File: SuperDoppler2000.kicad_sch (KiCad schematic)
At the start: 5 parts, among them U1 TPS7A0533PDBZ

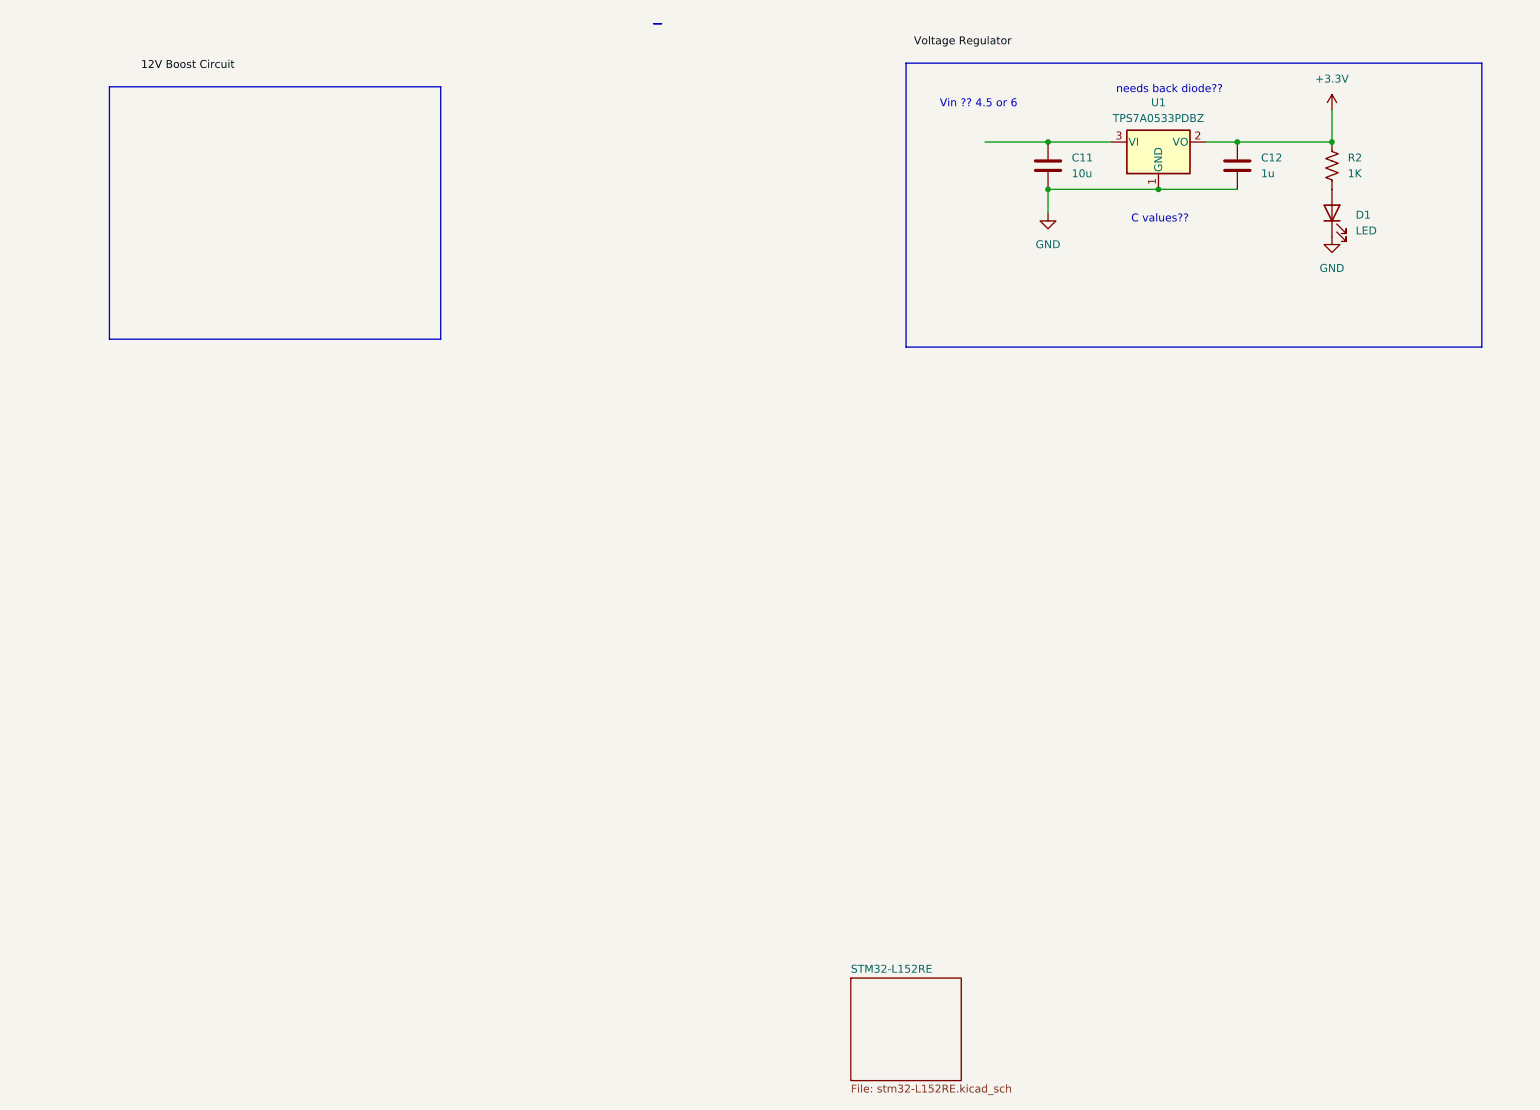
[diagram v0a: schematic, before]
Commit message: add buck
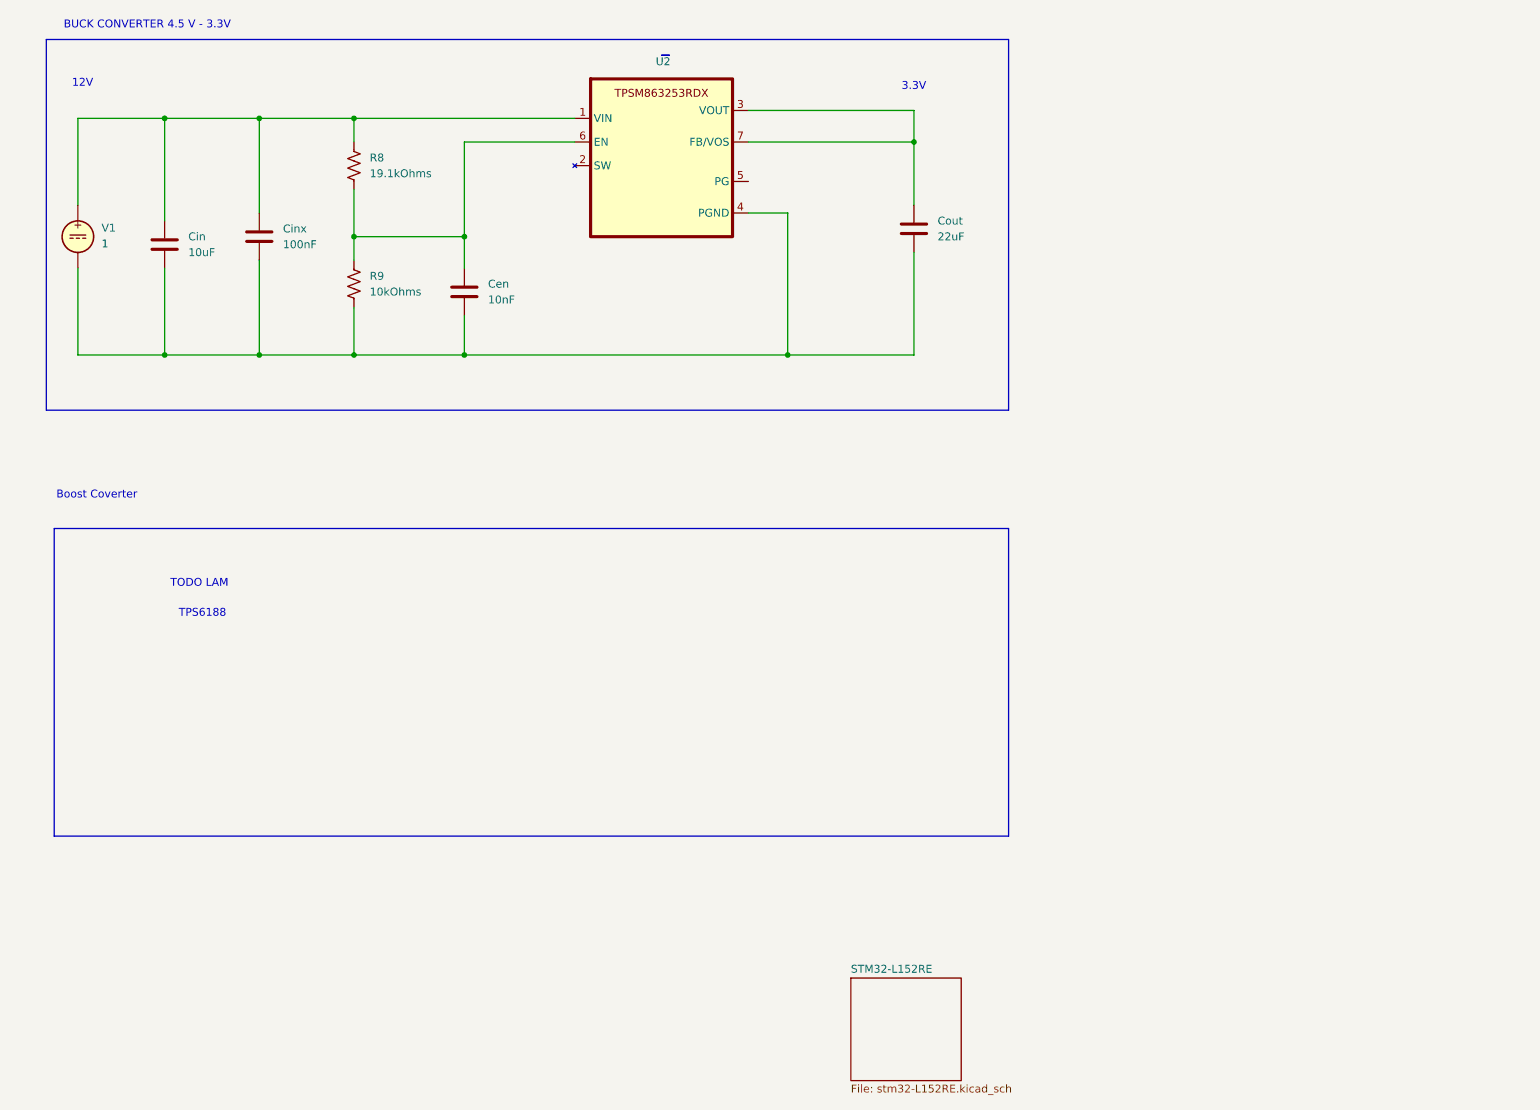
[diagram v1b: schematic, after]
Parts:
- removed C11: 10u, symbol Device:C
- removed C12: 1u, symbol Device:C
- removed D1: LED, symbol Device:LED
- removed R2: 1K, symbol Device:R_US
- removed U1: TPS7A0533PDBZ, Package_TO_SOT_SMD:SOT-23, symbol Regulator_Linear:TPS7A0533PDBZ
- added Cen: 10nF, symbol Device:C
- added Cin: 10uF, Capacitor_THT:C_Disc_D3.0mm_W1.6mm_P2.50mm, symbol Device:C
- added Cinx: 100nF, Capacitor_THT:C_Disc_D3.0mm_W1.6mm_P2.50mm, symbol Device:C
- added Cout: 22uF, symbol Device:C
- added R8: 19.1kOhms, symbol Device:R_US
- added R9: 10kOhms, symbol Device:R_US
- added U2: ~, symbol 2_Converter_DCDC:TPSM863253RDX
- added V1: 1, symbol Simulation_SPICE:VDC
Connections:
- new net: Cen.1, R8.2, R9.1, U2.6 (EN)
- new net: Cen.2, Cin.2, Cinx.2, Cout.2, R9.2, U2.4 (PGND), V1.2
- new net: Cin.1, Cinx.1, R8.1, U2.1 (VIN), V1.1
- new net: Cout.1, U2.3 (VOUT), U2.7 (FB/VOS)
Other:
- note added: "12V"
- note added: "3.3V"
- note added: "BUCK CONVERTER 4.5 V - 3.3V"
- note added: "Boost Coverter"
- note added: "TODO LAM"
- note added: "TPS6188"
- note removed: "C values??"
- note removed: "Vin ?? 4.5 or 6"
- note removed: "needs back diode??"

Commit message: Add files via upload
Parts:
- removed U2: ~, symbol 2_Converter_DCDC:TPSM863253RDX
- removed V1: 1, symbol Simulation_SPICE:VDC
- added C10: 68nF, Capacitor_THT:C_Disc_D3.0mm_W1.6mm_P2.50mm, symbol Device:C
- added C11: 47uF, Capacitor_THT:C_Disc_D3.0mm_W1.6mm_P2.50mm, symbol Device:C
- added C5: 10uF, Capacitor_THT:C_Disc_D3.0mm_W1.6mm_P2.50mm, symbol Device:C
- added C6, C7: 100nF, Capacitor_THT:C_Disc_D3.0mm_W1.6mm_P2.50mm, symbol Device:C
- added C8: 2.2uF, Capacitor_THT:C_Disc_D3.0mm_W1.6mm_P2.50mm, symbol Device:C
- added C9: 39nF, Capacitor_THT:C_Disc_D3.0mm_W1.6mm_P2.50mm, symbol Device:C
- added J3: JST PH, Connector_JST:JST_PH_B2B-PH-K_1x02_P2.00mm_Vertical, symbol Connector_Generic:Conn_01x02
- added L1: 4.7uH, symbol Device:L
- added R4: 26.7kOhms, symbol Device:R_US
- added R5: 931kOhms, symbol Device:R_US
- added R6: 48.7kOhms, symbol Device:R_US
- added U2: TPS61288RQQR, FootprintLibrary:RQQ0011A-MFG, symbol TPS61288RQQ:TPS61288RQQR
- added VR1: TPSM863253RDXR, FootprintLibrary:VREG_TPSM863253RDXR, symbol TPSM863253RDXR:TPSM863253RDXR
- renumbered Cin to C1, Cinx to C2, Cen to C3, Cout to C4, R8 to R1, R9 to R2
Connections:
- net at C3.1, R1.2, R2.1: now also VR1.6 (EN)
- net GND: now reaches C1.2, C2.2, C3.2, C4.2, R2.2
- net GND: now also C10.2, C11.2, C5.2, C7.2, C8.2, C9.2, J3.1 (Pin_1), R4.1, R6.2, U2.10 (AGND), U2.3 (PGND), VR1.4 (PGND)
- net +4.5V: now reaches C1.1, C2.1, R1.1
- net +4.5V: now also C5.1, C7.1, J3.2 (Pin_2), L1.1, U2.6 (EN), U2.7 (VIN), VR1.1 (VIN)
- net +3.3V: now reaches C4.1
- net +3.3V: now also VR1.3 (VOUT), VR1.7 (FB)
- new net: C9.1, R4.2
- new net: C8.1, U2.11 (VCC)
- new net: R5.2, R6.1, U2.1 (FB)
- new net: C6.1, L1.2, U2.9 (SW)
- new net: C6.2, U2.8 (BST)
- new net: C10.1, U2.2 (COMP)
- new net +12V: C11.1, R5.1, U2.5 (VOUT)
- no-connect marks 0 -> 2
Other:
- note added: "+3.3V?"
- note added: "BOOST CONVERTER 4.5 V - 12V"
- note added: "from 4.5? V battery"
- note removed: "12V"
- note removed: "3.3V"
- note removed: "Boost Coverter"
- note removed: "TODO LAM"
- note removed: "TPS6188"
- moved on the sheet: C1, C2, C3, C4, R1, R2

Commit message: updated schematic
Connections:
- net +4.5V renamed +4.5_or_+5
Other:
- note added: "4.5V from battery OR USB??"
- note added: "DIODE??"
- note added: "voltage reg??"
- note removed: "+3.3V?"
- note removed: "from 4.5? V battery"
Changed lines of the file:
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@@
 		(date "2026-01-28")
 	)
-	(text "+3.3V?"
-		(exclude_from_sim no)
-		(at 171.958 35.56 0)
+	(text "DIODE??"
+		(exclude_from_sim no)
+		(at 171.704 98.552 0)
 		(effects
 			(font
@@
 		)
 	)
-	(text "from 4.5? V battery"
-		(exclude_from_sim no)
-		(at 22.86 104.648 0)
+	(text "voltage reg??"
+		(exclude_from_sim no)
+		(at 28.956 59.69 0)
 		(effects
 			(font
@@
 		)
 	)
+	(text "4.5V from battery\nOR USB??"
+		(exclude_from_sim no)
+		(at 22.86 109.474 0)
+		(effects
+			(font
+				(size 1.27 1.27)
+				(color 255 0 255 1)
+			)
+		)
+	)
+	(text "DIODE??"
+		(exclude_from_sim no)
+		(at 149.606 36.83 0)
+		(effects
+			(font
+				(size 1.27 1.27)
+				(color 255 0 255 1)
+			)
+		)
+	)
 	(junction
 		(at 66.04 147.32)
@@
 	(junction
 		(at 77.47 147.32)
+		(diameter 0)
+		(color 0 0 0 0)
+	)
+	(junction
+		(at 158.75 34.29)
 		(diameter 0)
 		(color 0 0 0 0)
@@
 		(pts
 			(xy 44.45 100.33) (xy 44.45 147.32)
+		)
+		(stroke
+			(width 0)
+			(type default)
+		)
+	)
+	(wire
+		(pts
+			(xy 158.75 34.29) (xy 158.75 36.83)
 		)
 		(stroke
@@
 	)
 	(symbol
+		(lib_id "power:PWR_FLAG")
+		(at 158.75 34.29 90)
+		(unit 1)
+		(exclude_from_sim no)
+		(in_bom yes)
+		(on_board yes)
+		(dnp no)
+		(fields_autoplaced yes)
+		(property "Reference" "#FLG01"
+			(at 156.845 34.29 0)
+			(effects
+				(font
+					(size 1.27 1.27)
+				)
+				(hide yes)
+			)
+		)
+		(property "Value" "PWR_FLAG"
+			(at 154.94 34.2899 90)
+			(effects
+				(font
+					(size 1.27 1.27)
+				)
+				(justify left)
+			)
+		)
+		(property "Footprint" ""
+			(at 158.75 34.29 0)
+			(effects
+				(font
+					(size 1.27 1.27)
+				)
+				(hide yes)
+			)
+		)
+		(property "Datasheet" "~"
+			(at 158.75 34.29 0)
+			(effects
+				(font
+					(size 1.27 1.27)
+				)
+				(hide yes)
+			)
+		)
+		(property "Description" "Special symbol for telling ERC where power comes from"
+			(at 158.75 34.29 0)
+			(effects
+				(font
+					(size 1.27 1.27)
+				)
+				(hide yes)
+			)
+		)
+		(pin "1"
+		)
+		(instances
+			(project "SuperDoppler2000"
+				(path "/1cfe4a09-7a70-413b-8af3-1a4c6e9327a7"
+					(reference "#FLG01")
+					(unit 1)
+				)
+			)
+		)
+	)
+	(symbol
 		(lib_id "Device:R_US")
 		(at 86.36 63.5 0)
@@
 			)
 		)
-		(property "Value" "+4.5V"
+		(property "Value" "+4.5_or_+5"
 			(at 30.48 86.36 0)
 			(effects
@@
 	(symbol
 		(lib_id "power:+3.3V")
-		(at 158.75 36.83 0)
+		(at 158.75 34.29 0)
 		(unit 1)
 		(exclude_from_sim no)
@@
 		(fields_autoplaced yes)
 		(property "Reference" "#PWR025"
-			(at 158.75 40.64 0)
+			(at 158.75 38.1 0)
 			(effects
 				(font
@@
 		)
 		(property "Value" "+3.3V"
-			(at 158.75 31.75 0)
+			(at 158.75 29.21 0)
 			(effects
 				(font
@@
 		)
 		(property "Footprint" ""
-			(at 158.75 36.83 0)
+			(at 158.75 34.29 0)
 			(effects
 				(font
@@
 		)
 		(property "Datasheet" ""
-			(at 158.75 36.83 0)
+			(at 158.75 34.29 0)
 			(effects
 				(font
@@
 		)
 		(property "Description" "Power symbol creates a global label with name \"+3.3V\""
-			(at 158.75 36.83 0)
-			(effects
-				(font
+			(at 158.75 34.29 0)
+			(effects
+				(font

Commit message: Add files via upload
starting layout
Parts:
- removed C6: 100nF, Capacitor_THT:C_Disc_D3.0mm_W1.6mm_P2.50mm, symbol Device:C
- removed U2: TPS61288RQQR, FootprintLibrary:RQQ0011A-MFG, symbol TPS61288RQQ:TPS61288RQQR
- added CBST1: 100nF, Capacitor_THT:C_Disc_D3.0mm_W1.6mm_P2.50mm, symbol Device:C
- added D1: ESD9B5.0ST5G, Diode_SMD:D_SOD-323, symbol Diode:ESD9B5.0ST5G
- added D2, D3: BAT60A, Diode_SMD:D_SOD-323, symbol Diode:BAT60A
- added DLD2, LD1: LED_Red, LED_SMD:LED_0805_2012Metric_Pad1.15x1.40mm_HandSolder, symbol Device:LED
- added RLD1: 150, Resistor_SMD:R_0805_2012Metric_Pad1.20x1.40mm_HandSolder, symbol Device:R_US
- added RLD2: 500, Resistor_SMD:R_0805_2012Metric_Pad1.20x1.40mm_HandSolder, symbol Device:R_US
- added VR2: TPS61288RQQR, FootprintLibrary:RQQ0011A-MFG, symbol TPS61288RQQ:TPS61288RQQR
- Cen1: renamed from C3; footprint (none) -> Capacitor_THT:C_Disc_D3.0mm_W1.6mm_P2.50mm
- Cout1: renamed from C4; footprint (none) -> Capacitor_THT:C_Disc_D3.0mm_W1.6mm_P2.50mm
- L1: footprint (none) -> Inductor_SMD:L_0805_2012Metric
- R1: value 19.1kOhms -> 14.7k; footprint (none) -> Resistor_SMD:R_0805_2012Metric_Pad1.20x1.40mm_HandSolder
- R2: footprint (none) -> Resistor_SMD:R_0805_2012Metric_Pad1.20x1.40mm_HandSolder
- Rcomp1: renamed from R4; footprint (none) -> Resistor_SMD:R_0805_2012Metric_Pad1.20x1.40mm_HandSolder
- Rfbb1: renamed from R6; footprint (none) -> Resistor_SMD:R_0805_2012Metric_Pad1.20x1.40mm_HandSolder
- Rfbt1: renamed from R5; footprint (none) -> Resistor_SMD:R_0805_2012Metric_Pad1.20x1.40mm_HandSolder
- renumbered C9 to Ccomp1, C10 to Ccomp2, C1 to Cin1, C5 to Cin2, C2 to Cinx1, C7 to Cinx2, C11 to Cout2, C8 to Cvcc1, J3 to J1
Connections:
- net +12V: now also D3.1 (K); no longer Cout2.1, Rfbt1.1
- net +3.3V: now also D2.1 (K); no longer Cout1.1, VR1.3 (VOUT), VR1.7 (FB)
- net +4.5_or_+5: now also D1.2 (A2), VR2.6 (EN), VR2.7 (VIN)
- net GND: now also D1.1 (A1), DLD2.1 (K), LD1.1 (K), VR2.10 (AGND), VR2.3 (PGND); no longer Rcomp1.1
- net at Cvcc1.1: now also VR2.11 (VCC)
- net at Rfbb1.1, Rfbt1.2: now also VR2.1 (FB)
- net at L1.2: now also CBST1.1, VR2.4 (SW), VR2.9 (SW)
- net at Ccomp2.1: now also Rcomp1.1, VR2.2 (COMP)
- new net: DLD2.2 (A), RLD2.2
- new net: Cout2.1, D3.2 (A), RLD2.1, Rfbt1.1, VR2.5 (VOUT)
- new net: Cout1.1, D2.2 (A), RLD1.1, VR1.3 (VOUT), VR1.7 (FB)
- new net: LD1.2 (A), RLD1.2
- new net: CBST1.2, VR2.8 (BST)
- no-connect marks 2 -> 1
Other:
- note added: "2V @ 20mA"
- note added: "BAT60A is 10V 3A, need hight V?"
- note added: "R value seems too small"
- note added: "disc capacitors vs smd 0805??"
- note added: "placehodler footprint"
- note removed: "DIODE??"
- note removed: "voltage reg??"
- moved on the sheet: Ccomp1, Ccomp2, Cen1, Cin1, Cin2, Cinx1, Cinx2, Cout1, Cout2, Cvcc1, L1, Rcomp1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
